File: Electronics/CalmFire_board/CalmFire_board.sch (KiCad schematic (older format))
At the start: 11 parts

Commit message: [Electronics] Updated schematic, created project library with relay schematic & footprint. Schematic complete, PCB ready to deploy.
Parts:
- removed TH?: DHT22_Temperature_Humidity, symbol sensors:DHT22_Temperature_Humidity
- removed U?: ESP32-DEVKITC-32D, MODULE_ESP32-DEVKITC-32D, symbol ESP32-DEVKITC-32D:ESP32-DEVKITC-32D
- added Power_con1, Relay_con1: Screw_Terminal_01x02, Connector_Phoenix_MC_HighVoltage:PhoenixContact_MC_1,5_2-G-5.08_1x02_P5.08mm_Horizontal, symbol Connector:Screw_Terminal_01x02
- added Q1: IRF8301M, Package_TO_SOT_THT:TO-220-3_Vertical, symbol Transistor_FET:IRF8301M
- added R6: 100R, Resistor_THT:R_Axial_DIN0207_L6.3mm_D2.5mm_P10.16mm_Horizontal, symbol Device:R_Small
- added U1: ESP32-DEVKITC-32D, MODULE_ESP32-DEVKITC-32D, symbol ESP32-DEVKITC-32D:ESP32-DEVKITC-32D
- added U2: DS18B20, Package_TO_SOT_THT:TO-92_Inline, symbol Sensor_Temperature:DS18B20
- added U3: N4100_relay, CalmFire_board:N4100_relay, symbol CalmFire_board:N4100_relay
- added U4: DHT11, Sensor:Aosong_DHT11_5.5x12.0_P2.54mm, symbol Sensor:DHT11
- C1, C2: renamed from C?; footprint (none) -> Capacitor_THT:C_Disc_D3.0mm_W1.6mm_P2.50mm
- J1: renamed from J?; footprint (none) -> Connector_PinSocket_2.54mm:PinSocket_1x06_P2.54mm_Vertical
- R1, R2, R4, R5: renamed from R?; footprint (none) -> Resistor_THT:R_Axial_DIN0207_L6.3mm_D2.5mm_P10.16mm_Horizontal
- R3: renamed from R?; footprint (none) -> OptoDevice:R_LDR_5.0x4.1mm_P3mm_Vertical
- SW1: renamed from SW?; footprint (none) -> Rotary_Encoder:RotaryEncoder_Alps_EC11E-Switch_Vertical_H20mm
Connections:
- net +3V3: now also U1.1 (3V3)
- net +5V: now also Power_con1.1 (Pin_1), U1.19 (EXT_5V), U2.3 (VDD), U3.1, U4.1 (VCC)
- net CLK: now also U1.25 (IO21)
- net DIR: now also U1.27 (IO19)
- net GND: now also Power_con1.2 (Pin_2), Q1.3 (S), U1.14 (GND1), U1.20 (GND3), U1.26 (GND2), U2.1 (GND), U4.4 (GND)
- net at R3.2, R4.2: now also U1.6 (IO35)
- net CS renamed dispCS
- net dispCS: now also U1.12 (IO14)
- net Data renamed dispData
- net dispData: now also U1.10 (IO26)
- net LED renamed dispLED
- net dispLED: now also U1.15 (IO13)
- net WR renamed dispWR
- net dispWR: now also U1.11 (IO27)
- new net: Q1.1 (D), U3.2
- new net: Q1.2 (G), R6.1
- new net: Relay_con1.1 (Pin_1), U3.3
- new net: Relay_con1.2 (Pin_2), U3.5 (on)
- new net Relay: R6.2, U1.31 (IO16)
- new net Temperature: U1.30 (IO17), U2.2 (DQ), U4.2 (IO)
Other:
- moved on the sheet: R3, R4

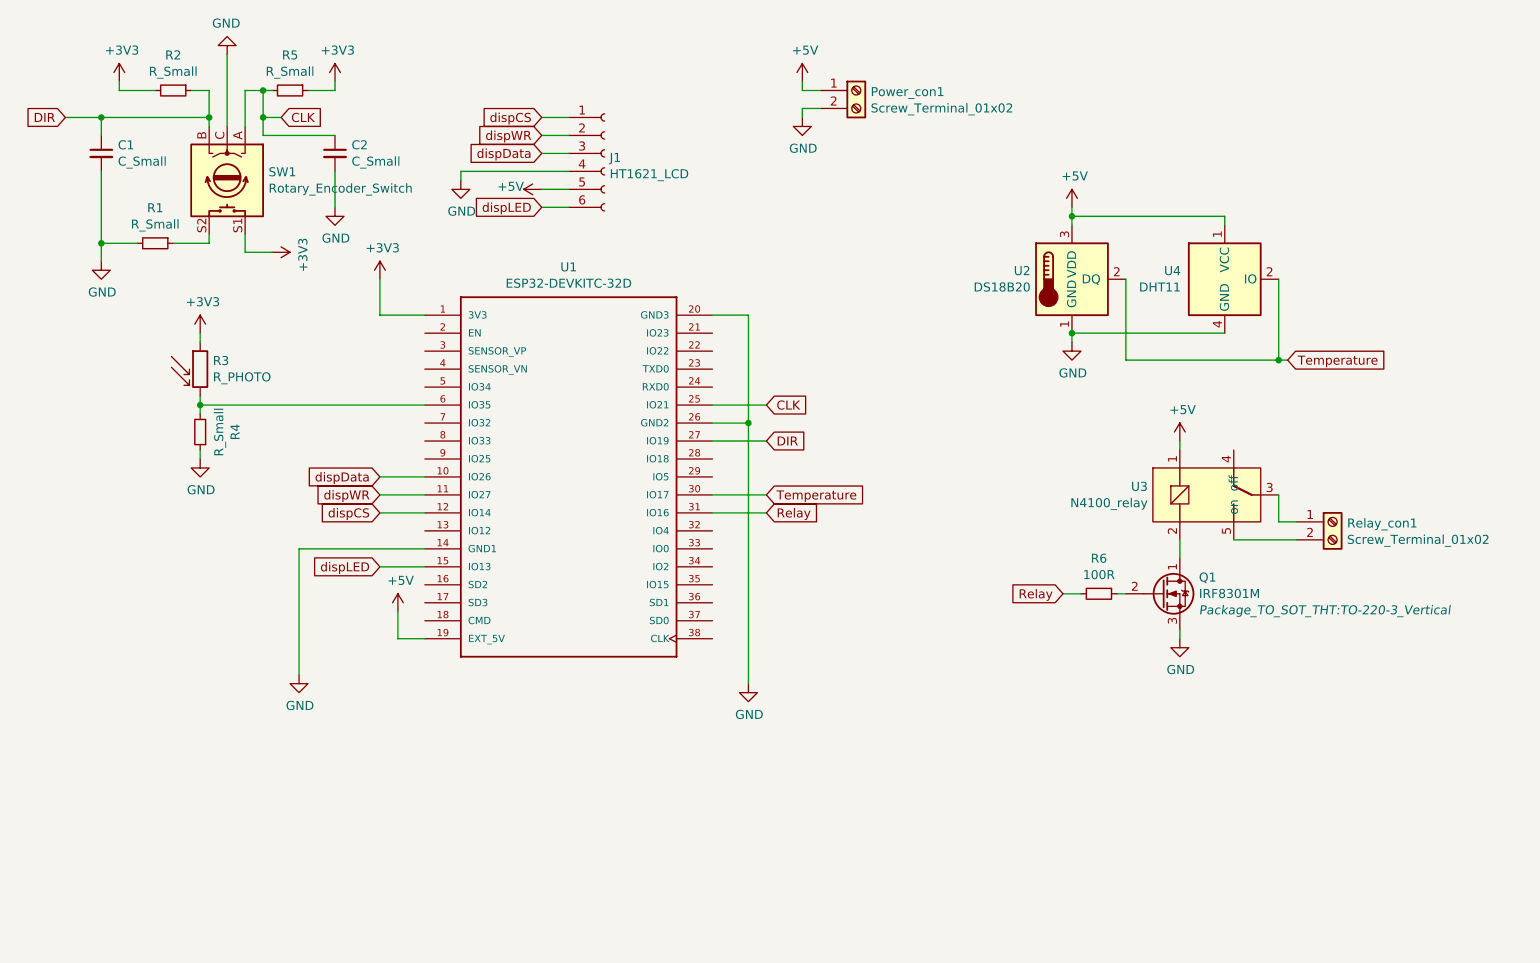
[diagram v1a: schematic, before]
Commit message: Created ht1621 display footprint. Added power capacitors, power polarity protection N-MOS. Changed temp sensors power to 3.3V and a pull-up on onewire.
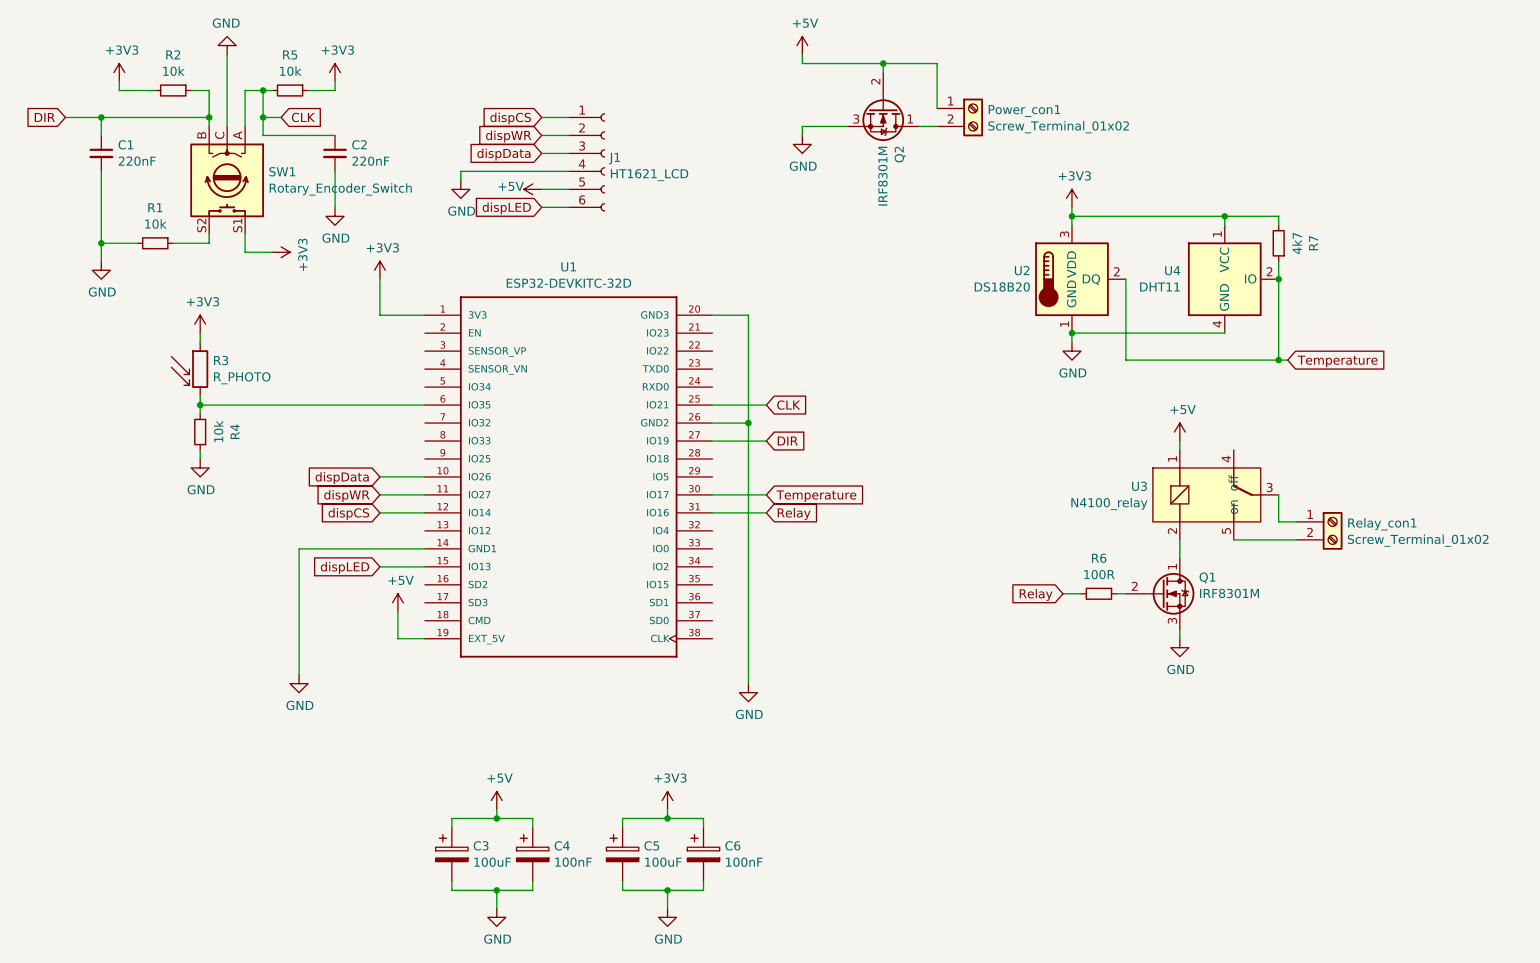
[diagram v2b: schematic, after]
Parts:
- added C3, C5: 100uF, Capacitor_THT:CP_Radial_D6.3mm_P2.50mm, symbol Device:CP
- added C4, C6: 100nF, Capacitor_THT:C_Disc_D3.0mm_W1.6mm_P2.50mm, symbol Device:CP
- added Q2: IRF8301M, Package_TO_SOT_THT:TO-220-3_Vertical, symbol Transistor_FET:IRF8301M
- added R7: 4k7, Resistor_THT:R_Axial_DIN0207_L6.3mm_D2.5mm_P10.16mm_Horizontal, symbol Device:R_Small
- C1, C2: value C_Small -> 220nF
- J1: footprint Connector_PinSocket_2.54mm:PinSocket_1x06_P2.54mm_Vertical -> CalmFire_board:ht1621
- R1, R2, R4, R5: value R_Small -> 10k
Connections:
- net +3V3: now also U2.3 (VDD), U4.1 (VCC), C5.1, C6.1, R7.2
- net +5V: now also C3.1, C4.1, Q2.2 (G); no longer U2.3 (VDD), U4.1 (VCC)
- net GND: now also C3.2, C4.2, C5.2, C6.2, Q2.3 (S); no longer Power_con1.2 (Pin_2)
- net Temperature: now also R7.1
- new net: Power_con1.2 (Pin_2), Q2.1 (D)
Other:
- moved on the sheet: Power_con1
